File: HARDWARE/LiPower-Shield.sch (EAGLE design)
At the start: 42 parts, among them U1 MAX17043G+U, U2 TPS61200, U3 MCP73831, U4 ARDUINO_R3_SHIELD, X1 USBSMD

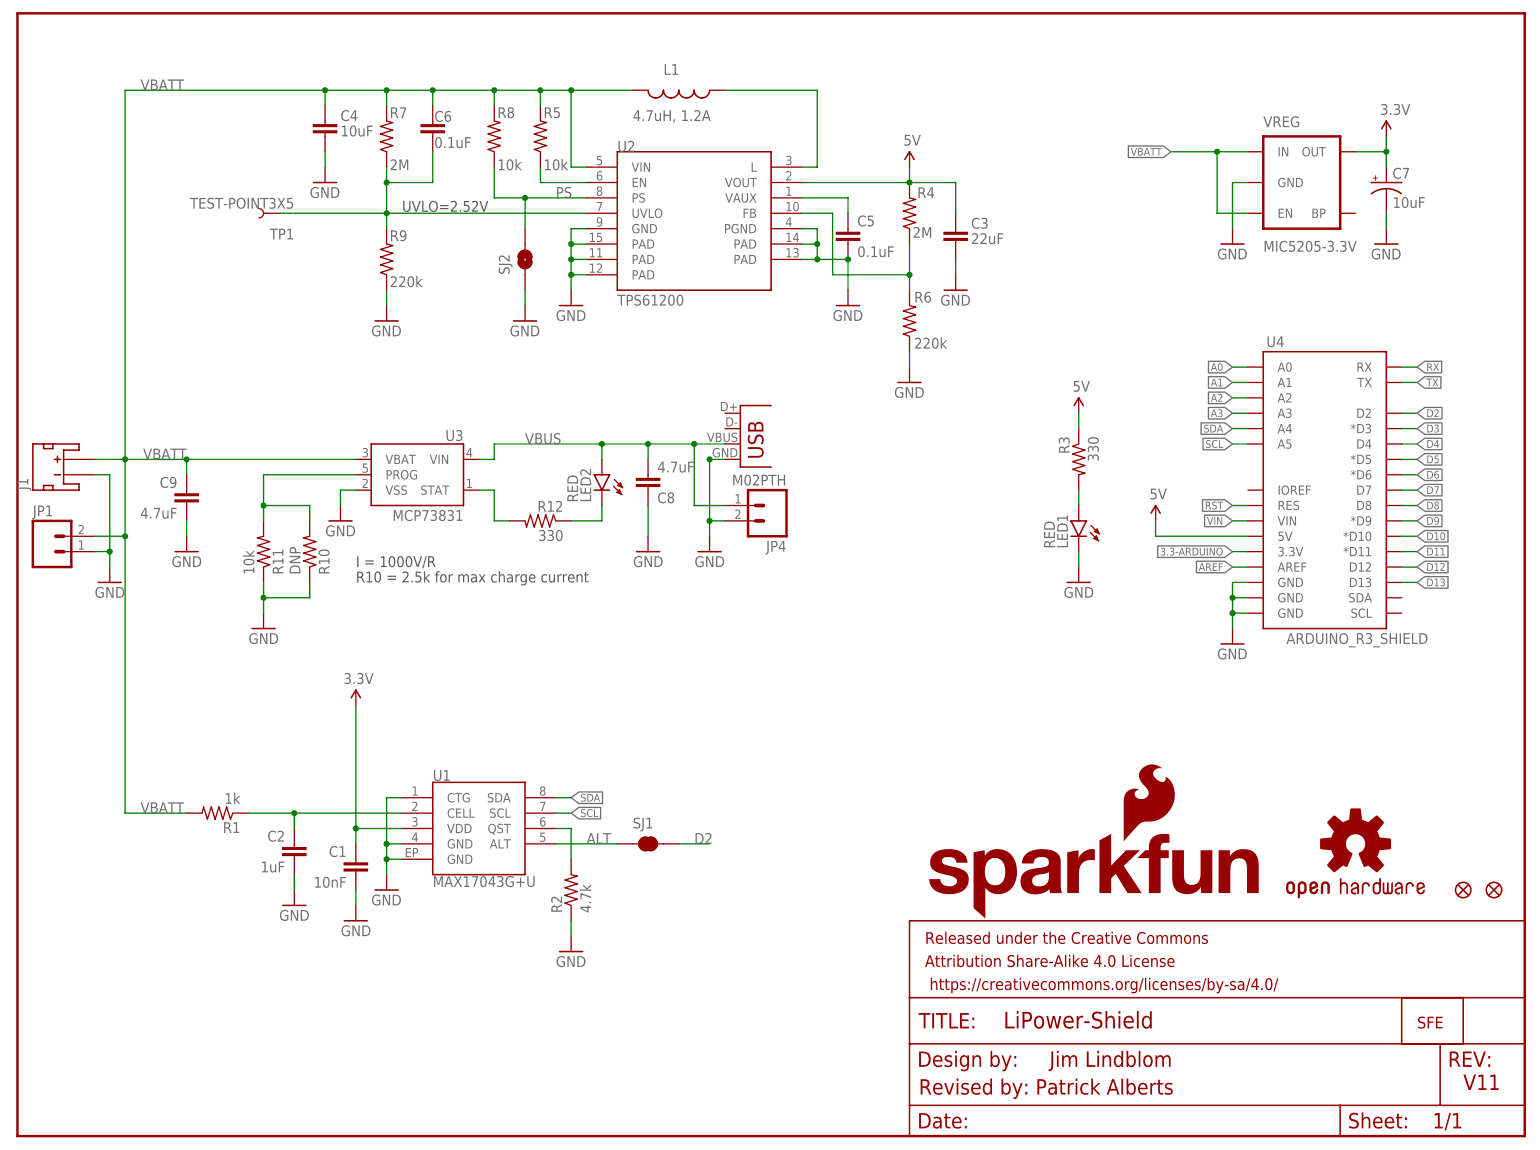
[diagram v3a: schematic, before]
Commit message: Added jumpers, isolated isp headers, trace reroutes
Added SCL SDA jumpers
Thermal relief for ground headers as well as changing all vias to
headers.
Added Test point for qc
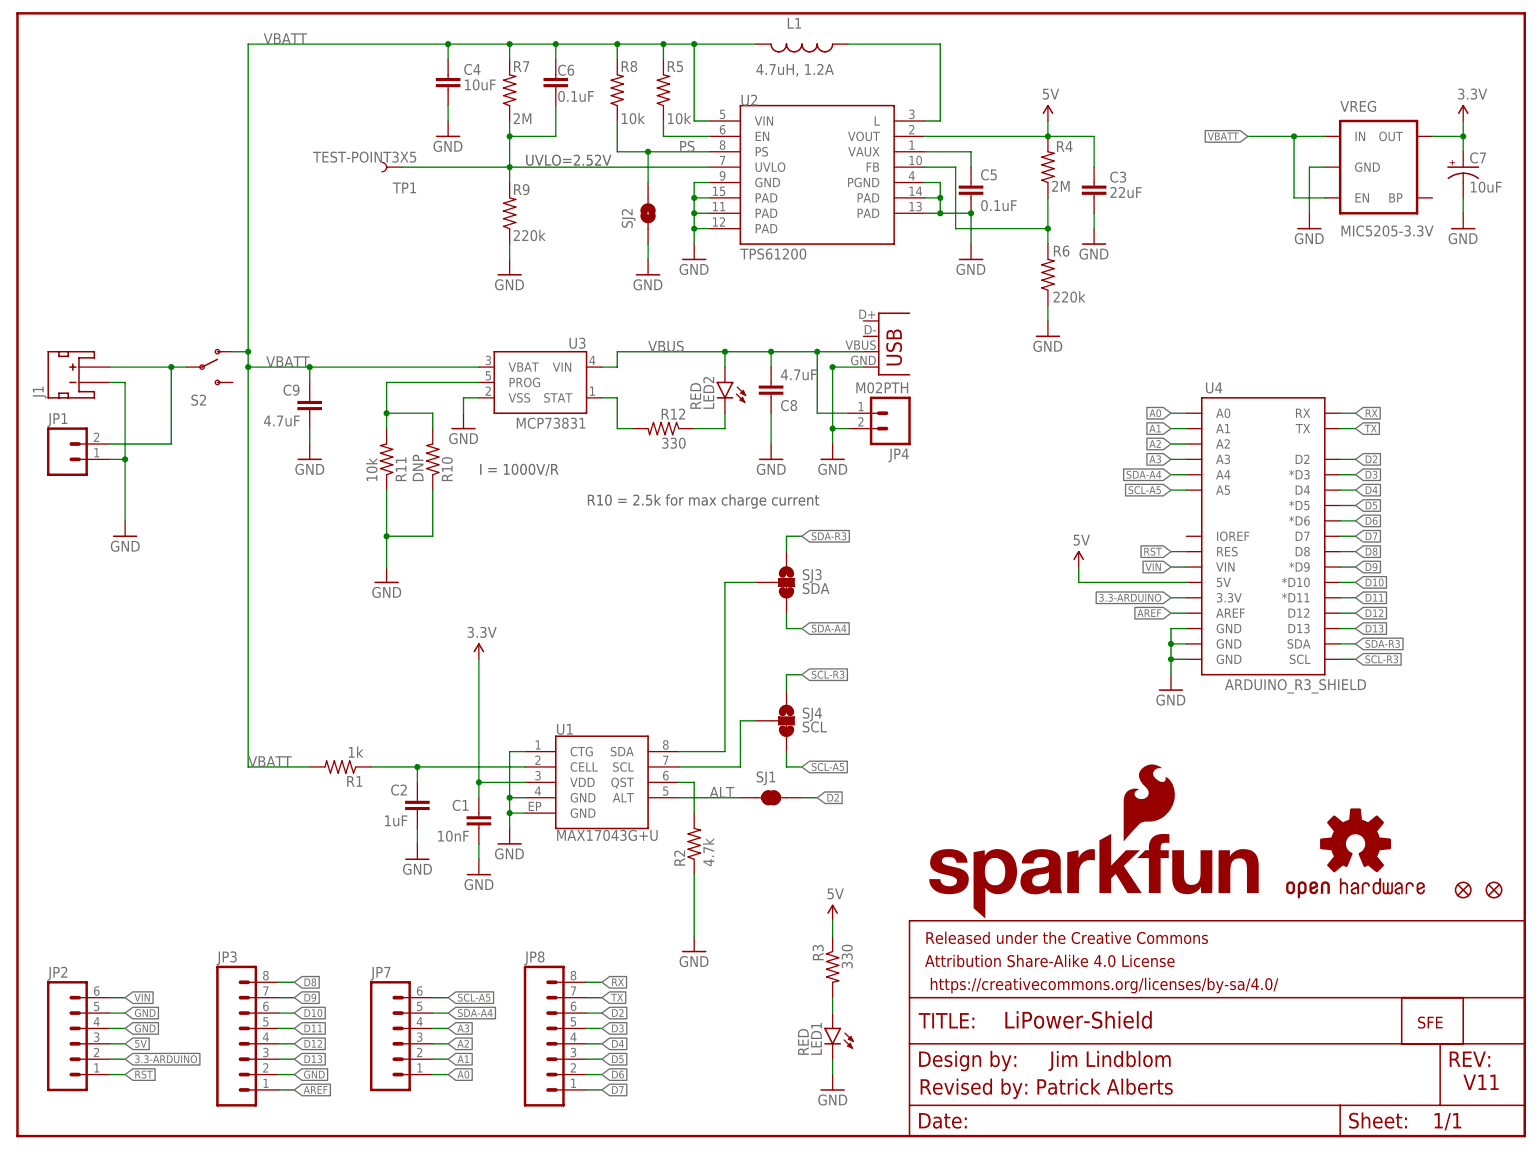
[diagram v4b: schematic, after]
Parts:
- added JP2, JP7: (no value), SparkFun-Connectors:M06NO_SILK
- added JP3, JP8: (no value), SparkFun-Connectors:M08NO_SILK
- added S2: (no value), SparkFun-Electromechanical:SWITCH-SPDT-SMD-A
- added SJ3: SDA, SparkFun-Passives:JUMPER-PAD-3-2OF3_NC_BY_TRACE
- added SJ4: SCL, SparkFun-Passives:JUMPER-PAD-3-2OF3_NC_BY_TRACE
- U2: device SparkFun:TPS61200 -> SparkFun-PowerIC:TPS61200
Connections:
- removed net SDA: U1.SDA, U4.A4
- new net N$20: SJ3.2, U1.SDA
- new net N$7: J1.+, JP1.2, S2.P
- new net SCL-A5: JP7.6, SJ4.3, U4.A5
- new net SCL-R3: SJ4.1, U4.SCL
- new net SDA-A4: JP7.5, SJ3.3, U4.A4
- new net SDA-R3: SJ3.1, U4.SDA
- net 3.3-ARDUINO: now also JP2.2
- net 5V: now also JP2.3
- net A0: now also JP7.1
- net A1: now also JP7.2
- net A2: now also JP7.3
- net A3: now also JP7.4
- net AREF: now also JP3.1
- net D10: now also JP3.6
- net D11: now also JP3.5
- net D12: now also JP3.4
- net D13: now also JP3.3
- net D2: now also JP8.6
- net D3: now also JP8.5
- net D4: now also JP8.4
- net D5: now also JP8.3
- net D6: now also JP8.2
- net D7: now also JP8.1
- net D8: now also JP3.8
- net D9: now also JP3.7
- net GND: now also JP2.4, JP2.5, JP3.2
- net RST: now also JP2.1
- net RX: now also JP8.8
- net SCL: now also SJ4.2; no longer U4.A5
- net TX: now also JP8.7
- net VBATT: now also S2.O; no longer J1.+, JP1.2
- net VIN: now also JP2.6
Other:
- moved on the sheet: C1, C2, C3, C4, C5, C6, C7, C8, C9, J1, JP1, JP4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

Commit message: Changed res values on the UVLO line.
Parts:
- R7: value 2M -> 2.2M; device SparkFun-Resistors:2MOHMS-1/10W-1%(0603) -> SparkFun-Resistors:2.2MOHM1/10W5%(0603)
- R9: value 220k -> 200k; device SparkFun-Resistors:220KOHM1/10W1%(0603) -> SparkFun-Resistors:200KOHM1/10W1%(0603)200K
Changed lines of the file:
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@@
 <part name="C6" library="SparkFun-Capacitors" deviceset="0.1UF-25V(+80/-20%)(0603)" device="" value="0.1uF"/>
 <part name="C5" library="SparkFun-Capacitors" deviceset="0.1UF-25V(+80/-20%)(0603)" device="" value="0.1uF"/>
-<part name="R7" library="SparkFun-Resistors" deviceset="2MOHMS-1/10W-1%(0603)" device="" value="2M"/>
-<part name="R9" library="SparkFun-Resistors" deviceset="220KOHM1/10W1%(0603)" device="" value="220k"/>
 <part name="R6" library="SparkFun-Resistors" deviceset="220KOHM1/10W1%(0603)" device="" value="220k"/>
 <part name="GND4" library="SparkFun" deviceset="GND" device=""/>
@@
 <part name="JP8" library="SparkFun-Connectors" deviceset="M08" device="NO_SILK"/>
 <part name="S2" library="SparkFun-Electromechanical" deviceset="SWITCH-SPDT" device="-SMD-A"/>
+<part name="R9" library="SparkFun-Resistors" deviceset="200KOHM1/10W1%(0603)" device="200K" value="200k"/>
+<part name="R7" library="SparkFun-Resistors" deviceset="2.2MOHM1/10W5%(0603)" device="" value="2.2M"/>
 </parts>
 <sheets>
@@
 </instance>
 <instance part="C5" gate="G$1" x="157.48" y="154.94"/>
-<instance part="R7" gate="G$1" x="81.28" y="172.72" smashed="yes" rot="R90">
-<attribute name="NAME" x="81.788" y="175.7426" size="1.778" layer="95"/>
-<attribute name="VALUE" x="81.788" y="167.132" size="1.778" layer="96"/>
-</instance>
-<instance part="R9" gate="G$1" x="81.28" y="152.4" smashed="yes" rot="R90">
-<attribute name="NAME" x="81.788" y="155.4226" size="1.778" layer="95"/>
-<attribute name="VALUE" x="81.788" y="147.828" size="1.778" layer="96"/>
-</instance>
 <instance part="R6" gate="G$1" x="170.18" y="142.24" smashed="yes" rot="R90">
 <attribute name="NAME" x="170.942" y="145.2626" size="1.778" layer="95"/>
@@
 <instance part="JP8" gate="G$1" x="88.9" y="15.24"/>
 <instance part="S2" gate="1" x="30.48" y="127"/>
+<instance part="R9" gate="G$1" x="81.28" y="152.4" rot="R90"/>
+<instance part="R7" gate="G$1" x="81.28" y="172.72" rot="R90"/>
 </instances>
 <busses>
@@
 <segment>
 <wire x1="81.28" y1="144.78" x2="81.28" y2="147.32" width="0.1524" layer="91"/>
+<pinref part="GND18" gate="1" pin="GND"/>
 <pinref part="R9" gate="G$1" pin="1"/>
-<pinref part="GND18" gate="1" pin="GND"/>
 </segment>
 <segment>
@@
 <label x="48.26" y="127" size="1.778" layer="95" rot="MR0"/>
 <label x="38.1" y="60.96" size="1.778" layer="95"/>
-<pinref part="R7" gate="G$1" pin="2"/>
 <pinref part="C4" gate="G$1" pin="1"/>
 <pinref part="C6" gate="G$1" pin="1"/>
@@
 <wire x1="35.56" y1="129.54" x2="38.1" y2="129.54" width="0.1524" layer="91"/>
 <junction x="38.1" y="129.54"/>
+<pinref part="R7" gate="G$1" pin="2"/>
 </segment>
 </net>
@@
 <pinref part="U2" gate="G$1" pin="UVLO"/>
 <pinref part="C6" gate="G$1" pin="2"/>
-<pinref part="R7" gate="G$1" pin="1"/>
-<pinref part="R9" gate="G$1" pin="2"/>
 <pinref part="TP1" gate="G$1" pin="1"/>
 <wire x1="63.5" y1="160.02" x2="81.28" y2="160.02" width="0.1524" layer="91"/>
-</segment>
-</net>
+<pinref part="R9" gate="G$1" pin="2"/>
+<pinref part="R7" gate="G$1" pin="1"/>
+</segment>
+</net>

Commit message: Changed UVLO voltage in SCH
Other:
- note added: "UVLO=2.75V"
- note removed: "UVLO=2.52V"
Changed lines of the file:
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@@
 <text x="76.2" y="109.22" size="1.778" layer="97">I = 1000V/R</text>
 <text x="93.98" y="104.14" size="1.778" layer="97">R10 = 2.5k for max charge current</text>
-<text x="83.82" y="160.274" size="1.778" layer="97">UVLO=2.52V</text>
+<text x="83.82" y="160.274" size="1.778" layer="97">UVLO=2.75V</text>
 <text x="238.76" y="7.62" size="2.54" layer="94">V11</text>
 <text x="170.434" y="11.43" size="2.54" layer="94">Jim Lindblom</text>

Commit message: Changed r7 back to 2m
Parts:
- R7: value 2.2M -> 2.0M; device SparkFun-Resistors:2.2MOHM1/10W5%(0603) -> SparkFun-Resistors:2MOHMS-1/10W-1%(0603)
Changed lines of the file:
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@@
 <part name="S2" library="SparkFun-Electromechanical" deviceset="SWITCH-SPDT" device="-SMD-A"/>
 <part name="R9" library="SparkFun-Resistors" deviceset="200KOHM1/10W1%(0603)" device="200K" value="200k"/>
-<part name="R7" library="SparkFun-Resistors" deviceset="2.2MOHM1/10W5%(0603)" device="" value="2.2M"/>
+<part name="R7" library="SparkFun-Resistors" deviceset="2MOHMS-1/10W-1%(0603)" device="" value="2.0M"/>
 </parts>
 <sheets>

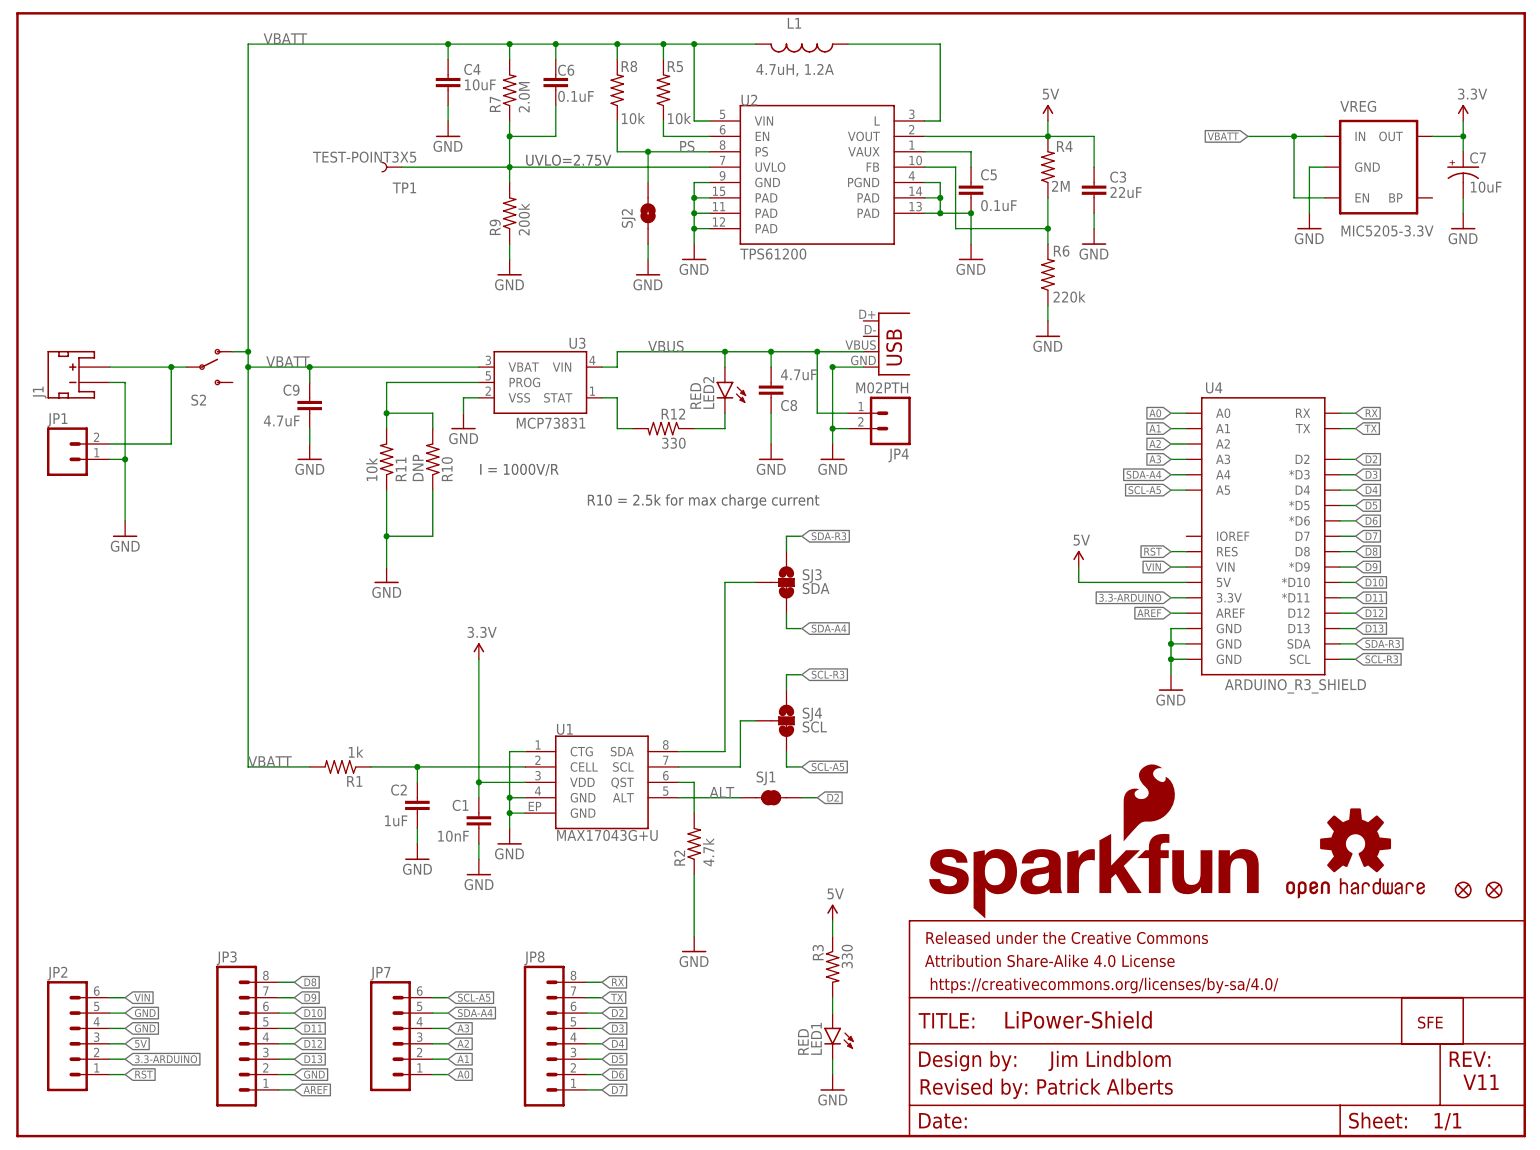
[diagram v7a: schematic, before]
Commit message: Added test point, Lines around Sch parts and Prod Att
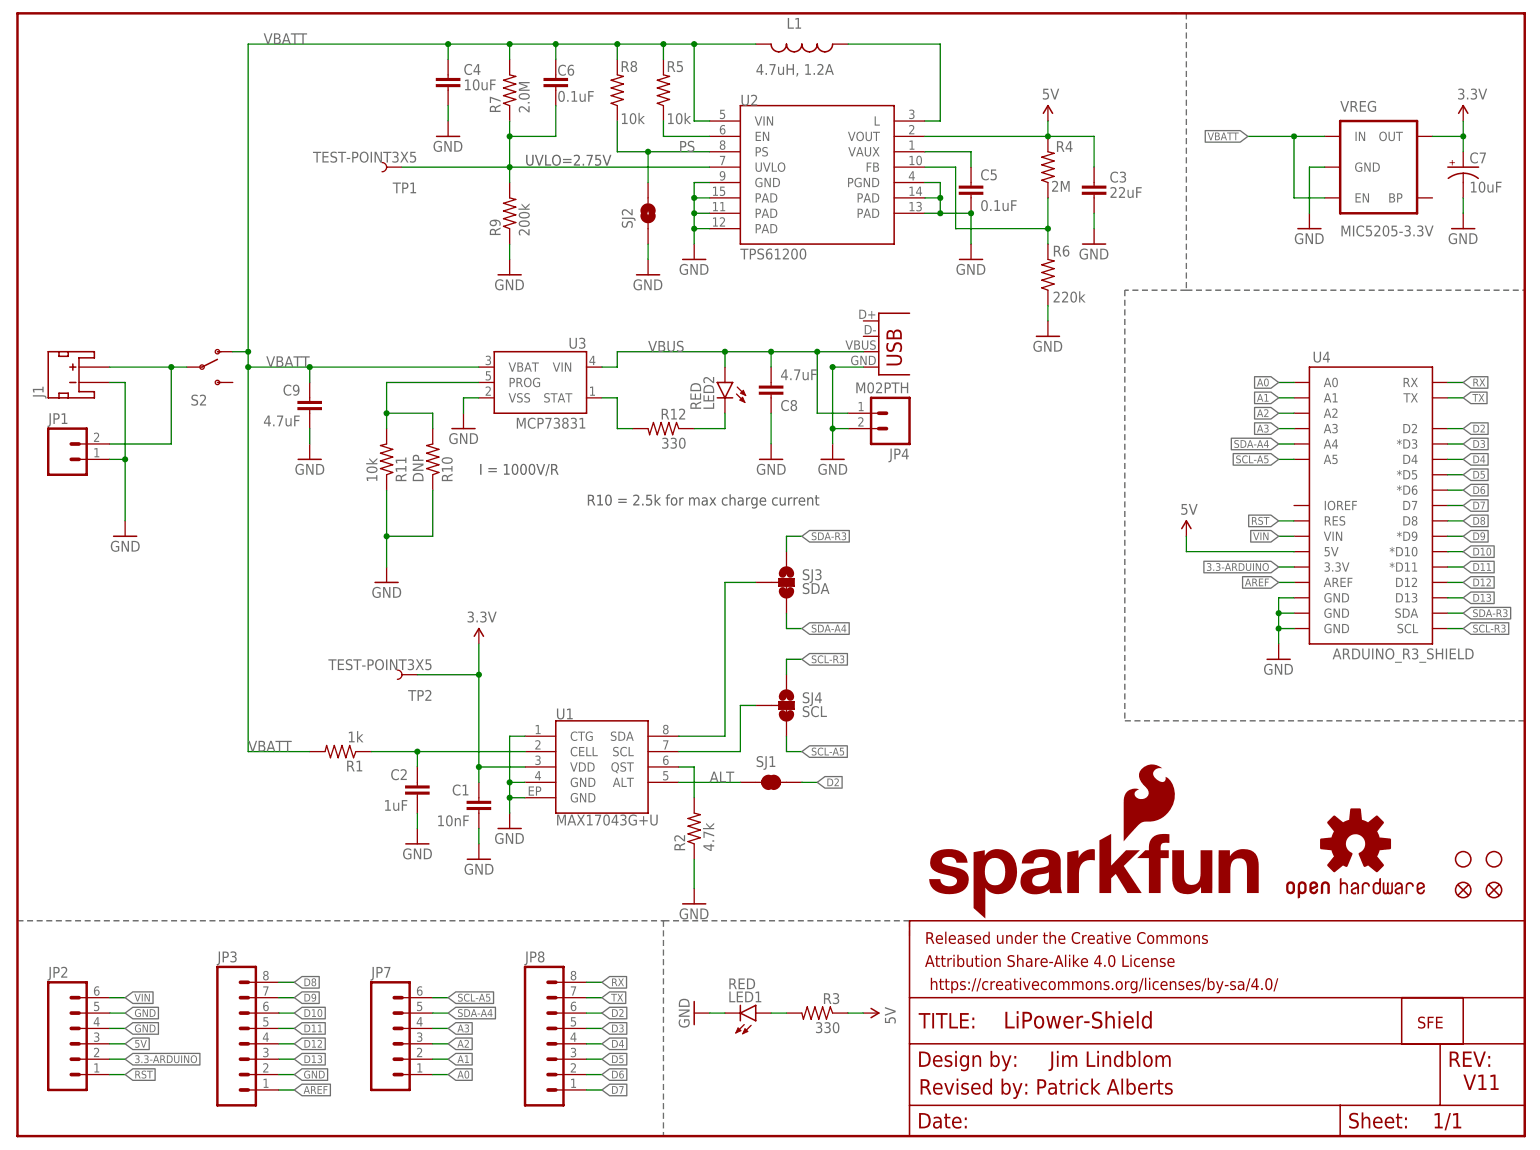
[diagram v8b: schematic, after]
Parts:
- added JP10, JP9: STAND-OFFTIGHT, SparkFun:STAND-OFFTIGHT
- added TP2: TEST-POINT3X5, SparkFun-Passives:TEST-POINT3X5
- C7: device SparkFun:CAP_POL1206 -> SparkFun-Capacitors:10UF-16V-10%(TANT)
- U3: device SparkFun:MCP73831 -> SparkFun-PowerIC:MCP73831
- VREG: device SparkFun:V_REG_LDOSMD -> SparkFun-PowerIC:MIC52053.3V
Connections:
- net 3.3V: now also TP2.1
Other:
- moved on the sheet: C1, C2, LED1, R1, R2, R3, SJ1, SJ4, U1, U4
